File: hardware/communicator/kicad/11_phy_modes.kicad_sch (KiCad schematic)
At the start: 4 parts, among them U26 SN74LVC2G125DCUR, U27 SN74LVC1G04DBVR

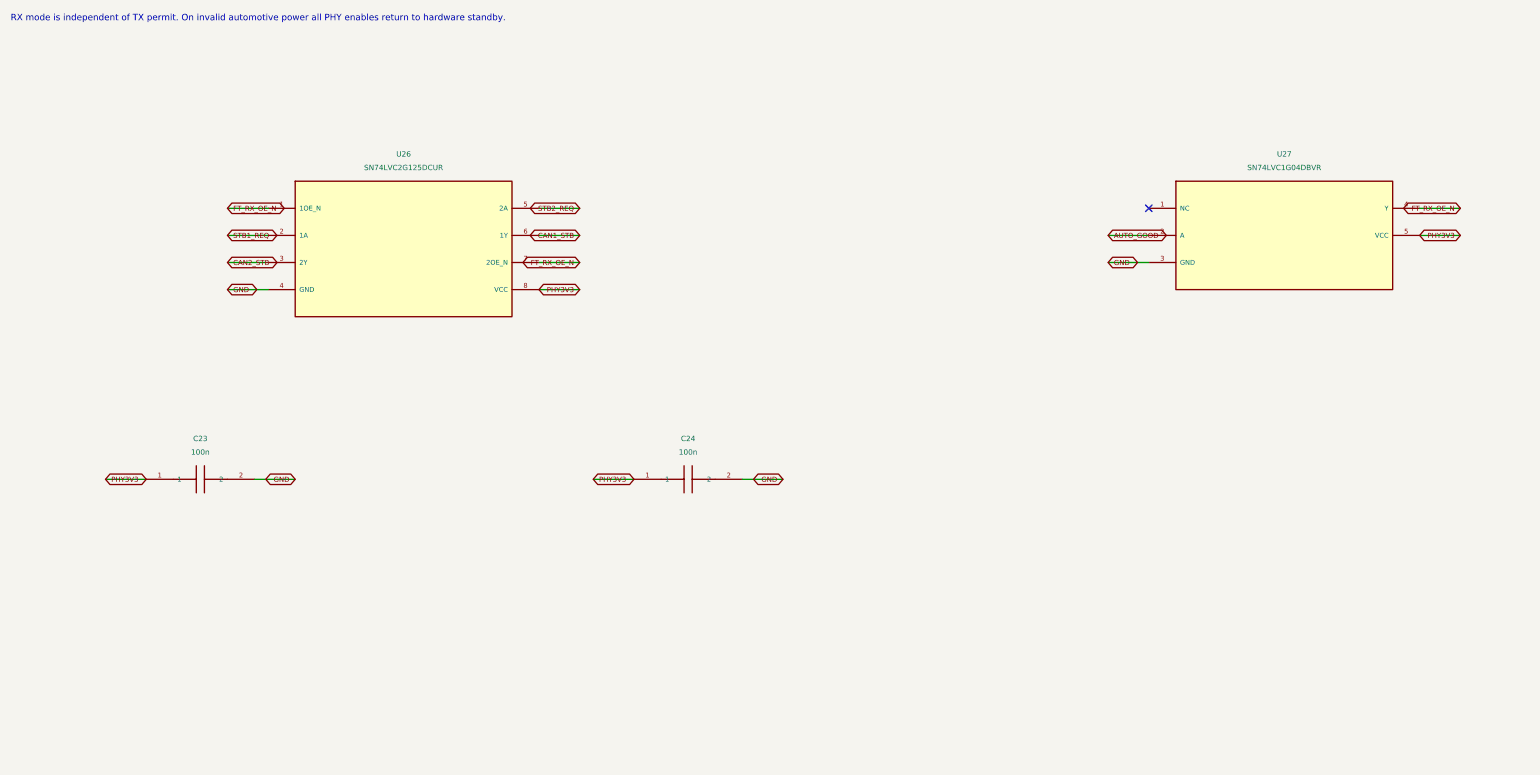
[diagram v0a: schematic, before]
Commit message: feat: add R1 detailed hardware and navigation protocol review candidate
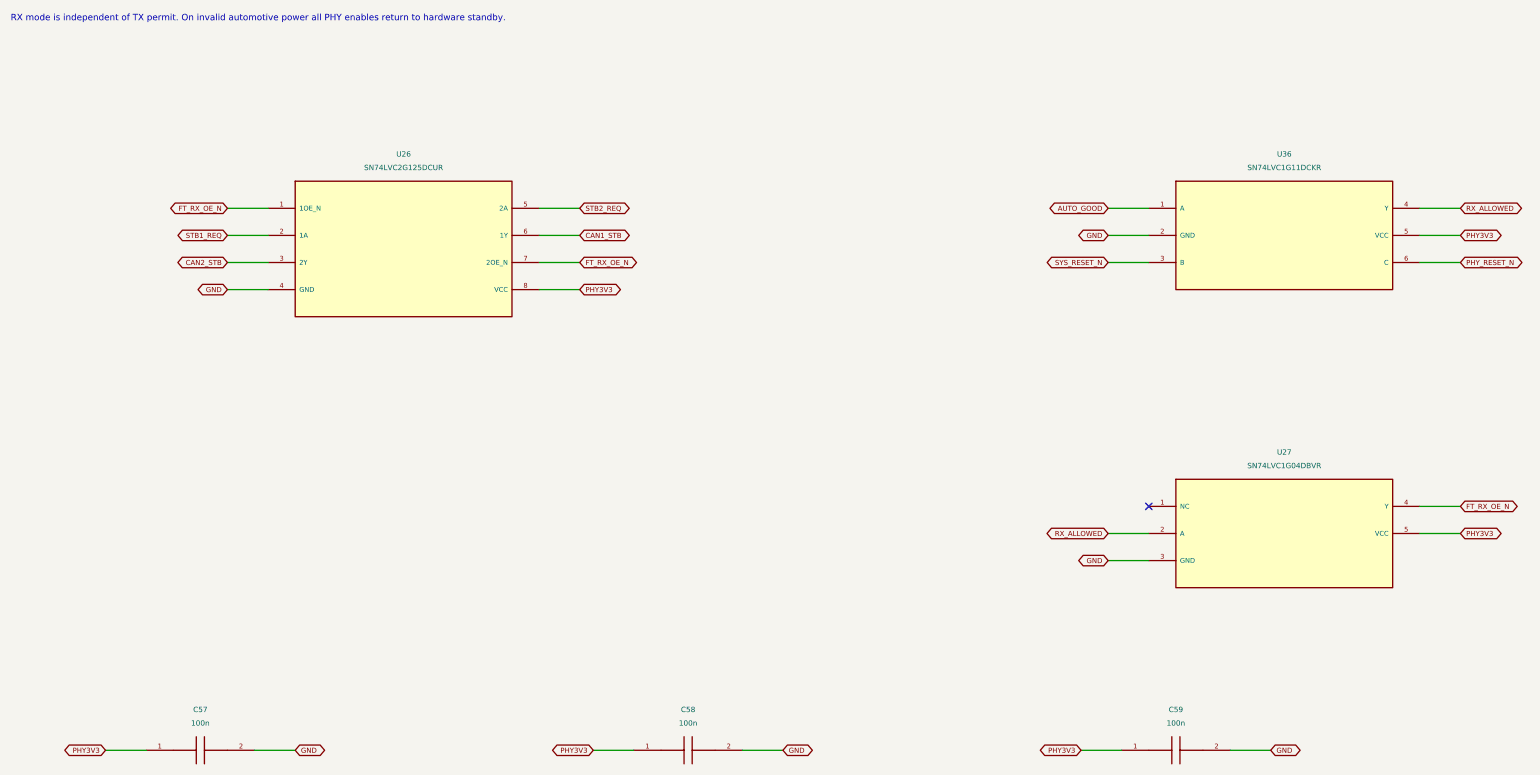
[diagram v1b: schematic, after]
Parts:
- removed C23: 100n, CANView:Capacitor_SMD__C_0402_1005Metric, symbol CANView:CANView_communicator_C23
- removed C24: 100n, CANView:Capacitor_SMD__C_0402_1005Metric, symbol CANView:CANView_communicator_C24
- added C57: 100n, CANView:Capacitor_SMD__C_0402_1005Metric, symbol CANView:CANView_communicator_C57
- added C58: 100n, CANView:Capacitor_SMD__C_0402_1005Metric, symbol CANView:CANView_communicator_C58
- added C59: 100n, CANView:Capacitor_SMD__C_0402_1005Metric, symbol CANView:CANView_communicator_C59
- added U36: SN74LVC1G11DCKR, CANView:Package_TO_SOT_SMD__SOT-363_SC-70-6, symbol CANView:CANView_communicator_U36
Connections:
- net AUTO_GOOD: now also U36.1 (A); no longer U27.2 (A)
- net GND: now also C57.2, C58.2, C59.2, U36.2 (GND)
- net PHY3V3: now also C57.1, C58.1, C59.1, U36.5 (VCC)
- new net PHY_RESET_N: U36.6 (C)
- new net RX_ALLOWED: U27.2 (A), U36.4 (Y)
- new net SYS_RESET_N: U36.3 (B)
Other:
- moved on the sheet: U27

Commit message: fix: close hardware rail-fault paths and sensor contract gaps
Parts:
- removed C57: 100n, CANView:Capacitor_SMD__C_0402_1005Metric, symbol CANView:CANView_communicator_C57
- removed C58: 100n, CANView:Capacitor_SMD__C_0402_1005Metric, symbol CANView:CANView_communicator_C58
- added C60: 100n, CANView:Capacitor_SMD__C_0402_1005Metric, symbol CANView:CANView_communicator_C60
- added C61: 100n, CANView:Capacitor_SMD__C_0402_1005Metric, symbol CANView:CANView_communicator_C61
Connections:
- net GND: now also C60.2, C61.2
- net PHY3V3: now also C60.1, C61.1
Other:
- moved on the sheet: C59
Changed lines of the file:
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@@
 (wire (pts (xy 279.4000 60.9600) (xy 287.0200 60.9600)) (stroke (width 0) (type default)))
 (global_label "PHY_RESET_N" (shape bidirectional) (at 287.0200 60.9600 0) (effects (font (size 0.95 0.95)) (justify left)) (property "Intersheetrefs" "${INTERSHEET_REFS}" (at 287.0200 60.9600 0) (hide yes) (effects (font (size 1.0 1.0)) )))
-(symbol (lib_id "CANView:CANView_communicator_C57") (at 50.8000 152.4000 0) (unit 1) (in_bom yes) (on_board yes) (dnp no) (property "Reference" "C57" (at 50.8000 144.7800 0)  (effects (font (size 1.0 1.0)) ))(property "Value" "100n" (at 50.8000 147.3200 0)  (effects (font (size 1.0 1.0)) ))(property "Footprint" "CANView:Capacitor_SMD__C_0402_1005Metric" (at 50.8000 152.4000 0) (hide yes) (effects (font (size 1.0 1.0)) ))(property "MPN" "GEN-C-0402-100n-16V-X7R" (at 50.8000 152.4000 0) (hide yes) (effects (font (size 1.0 1.0)) ))(property "Specification" "16V; ±10%; X7R; -55..125C; verify effective capacitance under DC bias" (at 50.8000 152.4000 0) (hide yes) (effects (font (size 1.0 1.0)) ))(property "Source" "" (at 50.8000 152.4000 0) (hide yes) (effects (font (size 1.0 1.0)) ))(property "Assembly" "FIT" (at 50.8000 152.4000 0) (hide yes) (effects (font (size 1.0 1.0)) ))(instances (project "communicator" (path "/c8ff26d1-0b80-520e-ae3f-45aa29bfe092/b6f15b90-8f25-5f05-b470-a22f12126907" (reference "C57") (unit 1)))))
+(symbol (lib_id "CANView:CANView_communicator_C59") (at 50.8000 152.4000 0) (unit 1) (in_bom yes) (on_board yes) (dnp no) (property "Reference" "C59" (at 50.8000 144.7800 0)  (effects (font (size 1.0 1.0)) ))(property "Value" "100n" (at 50.8000 147.3200 0)  (effects (font (size 1.0 1.0)) ))(property "Footprint" "CANView:Capacitor_SMD__C_0402_1005Metric" (at 50.8000 152.4000 0) (hide yes) (effects (font (size 1.0 1.0)) ))(property "MPN" "GEN-C-0402-100n-16V-X7R" (at 50.8000 152.4000 0) (hide yes) (effects (font (size 1.0 1.0)) ))(property "Specification" "16V; ±10%; X7R; -55..125C; verify effective capacitance under DC bias" (at 50.8000 152.4000 0) (hide yes) (effects (font (size 1.0 1.0)) ))(property "Source" "" (at 50.8000 152.4000 0) (hide yes) (effects (font (size 1.0 1.0)) ))(property "Assembly" "FIT" (at 50.8000 152.4000 0) (hide yes) (effects (font (size 1.0 1.0)) ))(instances (project "communicator" (path "/c8ff26d1-0b80-520e-ae3f-45aa29bfe092/b6f15b90-8f25-5f05-b470-a22f12126907" (reference "C59") (unit 1)))))
 (wire (pts (xy 40.6400 152.4000) (xy 33.0200 152.4000)) (stroke (width 0) (type default)))
 (global_label "PHY3V3" (shape bidirectional) (at 33.0200 152.4000 180) (effects (font (size 0.95 0.95)) (justify right)) (property "Intersheetrefs" "${INTERSHEET_REFS}" (at 33.0200 152.4000 0) (hide yes) (effects (font (size 1.0 1.0)) )))
@@
 (wire (pts (xy 279.4000 111.7600) (xy 287.0200 111.7600)) (stroke (width 0) (type default)))
 (global_label "PHY3V3" (shape bidirectional) (at 287.0200 111.7600 0) (effects (font (size 0.95 0.95)) (justify left)) (property "Intersheetrefs" "${INTERSHEET_REFS}" (at 287.0200 111.7600 0) (hide yes) (effects (font (size 1.0 1.0)) )))
-(symbol (lib_id "CANView:CANView_communicator_C58") (at 142.2400 152.4000 0) (unit 1) (in_bom yes) (on_board yes) (dnp no) (property "Reference" "C58" (at 142.2400 144.7800 0)  (effects (font (size 1.0 1.0)) ))(property "Value" "100n" (at 142.2400 147.3200 0)  (effects (font (size 1.0 1.0)) ))(property "Footprint" "CANView:Capacitor_SMD__C_0402_1005Metric" (at 142.2400 152.4000 0) (hide yes) (effects (font (size 1.0 1.0)) ))(property "MPN" "GEN-C-0402-100n-16V-X7R" (at 142.2400 152.4000 0) (hide yes) (effects (font (size 1.0 1.0)) ))(property "Specification" "16V; ±10%; X7R; -55..125C; verify effective capacitance under DC bias" (at 142.2400 152.4000 0) (hide yes) (effects (font (size 1.0 1.0)) ))(property "Source" "" (at 142.2400 152.4000 0) (hide yes) (effects (font (size 1.0 1.0)) ))(property "Assembly" "FIT" (at 142.2400 152.4000 0) (hide yes) (effects (font (size 1.0 1.0)) ))(instances (project "communicator" (path "/c8ff26d1-0b80-520e-ae3f-45aa29bfe092/b6f15b90-8f25-5f05-b470-a22f12126907" (reference "C58") (unit 1)))))
+(symbol (lib_id "CANView:CANView_communicator_C60") (at 142.2400 152.4000 0) (unit 1) (in_bom yes) (on_board yes) (dnp no) (property "Reference" "C60" (at 142.2400 144.7800 0)  (effects (font (size 1.0 1.0)) ))(property "Value" "100n" (at 142.2400 147.3200 0)  (effects (font (size 1.0 1.0)) ))(property "Footprint" "CANView:Capacitor_SMD__C_0402_1005Metric" (at 142.2400 152.4000 0) (hide yes) (effects (font (size 1.0 1.0)) ))(property "MPN" "GEN-C-0402-100n-16V-X7R" (at 142.2400 152.4000 0) (hide yes) (effects (font (size 1.0 1.0)) ))(property "Specification" "16V; ±10%; X7R; -55..125C; verify effective capacitance under DC bias" (at 142.2400 152.4000 0) (hide yes) (effects (font (size 1.0 1.0)) ))(property "Source" "" (at 142.2400 152.4000 0) (hide yes) (effects (font (size 1.0 1.0)) ))(property "Assembly" "FIT" (at 142.2400 152.4000 0) (hide yes) (effects (font (size 1.0 1.0)) ))(instances (project "communicator" (path "/c8ff26d1-0b80-520e-ae3f-45aa29bfe092/b6f15b90-8f25-5f05-b470-a22f12126907" (reference "C60") (unit 1)))))
 (wire (pts (xy 132.0800 152.4000) (xy 124.4600 152.4000)) (stroke (width 0) (type default)))
 (global_label "PHY3V3" (shape bidirectional) (at 124.4600 152.4000 180) (effects (font (size 0.95 0.95)) (justify right)) (property "Intersheetrefs" "${INTERSHEET_REFS}" (at 124.4600 152.4000 0) (hide yes) (effects (font (size 1.0 1.0)) )))
 (wire (pts (xy 152.4000 152.4000) (xy 160.0200 152.4000)) (stroke (width 0) (type default)))
 (global_label "GND" (shape bidirectional) (at 160.0200 152.4000 0) (effects (font (size 0.95 0.95)) (justify left)) (property "Intersheetrefs" "${INTERSHEET_REFS}" (at 160.0200 152.4000 0) (hide yes) (effects (font (size 1.0 1.0)) )))
-(symbol (lib_id "CANView:CANView_communicator_C59") (at 233.6800 152.4000 0) (unit 1) (in_bom yes) (on_board yes) (dnp no) (property "Reference" "C59" (at 233.6800 144.7800 0)  (effects (font (size 1.0 1.0)) ))(property "Value" "100n" (at 233.6800 147.3200 0)  (effects (font (size 1.0 1.0)) ))(property "Footprint" "CANView:Capacitor_SMD__C_0402_1005Metric" (at 233.6800 152.4000 0) (hide yes) (effects (font (size 1.0 1.0)) ))(property "MPN" "GEN-C-0402-100n-16V-X7R" (at 233.6800 152.4000 0) (hide yes) (effects (font (size 1.0 1.0)) ))(property "Specification" "16V; ±10%; X7R; -55..125C; verify effective capacitance under DC bias" (at 233.6800 152.4000 0) (hide yes) (effects (font (size 1.0 1.0)) ))(property "Source" "" (at 233.6800 152.4000 0) (hide yes) (effects (font (size 1.0 1.0)) ))(property "Assembly" "FIT" (at 233.6800 152.4000 0) (hide yes) (effects (font (size 1.0 1.0)) ))(instances (project "communicator" (path "/c8ff26d1-0b80-520e-ae3f-45aa29bfe092/b6f15b90-8f25-5f05-b470-a22f12126907" (reference "C59") (unit 1)))))
+(symbol (lib_id "CANView:CANView_communicator_C61") (at 233.6800 152.4000 0) (unit 1) (in_bom yes) (on_board yes) (dnp no) (property "Reference" "C61" (at 233.6800 144.7800 0)  (effects (font (size 1.0 1.0)) ))(property "Value" "100n" (at 233.6800 147.3200 0)  (effects (font (size 1.0 1.0)) ))(property "Footprint" "CANView:Capacitor_SMD__C_0402_1005Metric" (at 233.6800 152.4000 0) (hide yes) (effects (font (size 1.0 1.0)) ))(property "MPN" "GEN-C-0402-100n-16V-X7R" (at 233.6800 152.4000 0) (hide yes) (effects (font (size 1.0 1.0)) ))(property "Specification" "16V; ±10%; X7R; -55..125C; verify effective capacitance under DC bias" (at 233.6800 152.4000 0) (hide yes) (effects (font (size 1.0 1.0)) ))(property "Source" "" (at 233.6800 152.4000 0) (hide yes) (effects (font (size 1.0 1.0)) ))(property "Assembly" "FIT" (at 233.6800 152.4000 0) (hide yes) (effects (font (size 1.0 1.0)) ))(instances (project "communicator" (path "/c8ff26d1-0b80-520e-ae3f-45aa29bfe092/b6f15b90-8f25-5f05-b470-a22f12126907" (reference "C61") (unit 1)))))
 (wire (pts (xy 223.5200 152.4000) (xy 215.9000 152.4000)) (stroke (width 0) (type default)))
 (global_label "PHY3V3" (shape bidirectional) (at 215.9000 152.4000 180) (effects (font (size 0.95 0.95)) (justify right)) (property "Intersheetrefs" "${INTERSHEET_REFS}" (at 215.9000 152.4000 0) (hide yes) (effects (font (size 1.0 1.0)) )))

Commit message: Design independent OTA recovery and update N16R8 hardware
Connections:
- net SYS_RESET_N renamed RUN_ALLOWED
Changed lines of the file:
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@@
 (global_label "GND" (shape bidirectional) (at 220.9800 55.8800 180) (effects (font (size 0.95 0.95)) (justify right)) (property "Intersheetrefs" "${INTERSHEET_REFS}" (at 220.9800 55.8800 0) (hide yes) (effects (font (size 1.0 1.0)) )))
 (wire (pts (xy 228.6000 60.9600) (xy 220.9800 60.9600)) (stroke (width 0) (type default)))
-(global_label "SYS_RESET_N" (shape bidirectional) (at 220.9800 60.9600 180) (effects (font (size 0.95 0.95)) (justify right)) (property "Intersheetrefs" "${INTERSHEET_REFS}" (at 220.9800 60.9600 0) (hide yes) (effects (font (size 1.0 1.0)) )))
+(global_label "RUN_ALLOWED" (shape bidirectional) (at 220.9800 60.9600 180) (effects (font (size 0.95 0.95)) (justify right)) (property "Intersheetrefs" "${INTERSHEET_REFS}" (at 220.9800 60.9600 0) (hide yes) (effects (font (size 1.0 1.0)) )))
 (wire (pts (xy 279.4000 50.8000) (xy 287.0200 50.8000)) (stroke (width 0) (type default)))
 (global_label "RX_ALLOWED" (shape bidirectional) (at 287.0200 50.8000 0) (effects (font (size 0.95 0.95)) (justify left)) (property "Intersheetrefs" "${INTERSHEET_REFS}" (at 287.0200 50.8000 0) (hide yes) (effects (font (size 1.0 1.0)) )))
